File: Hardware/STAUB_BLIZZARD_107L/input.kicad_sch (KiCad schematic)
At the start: 26 parts, among them IC2 MC33978AES

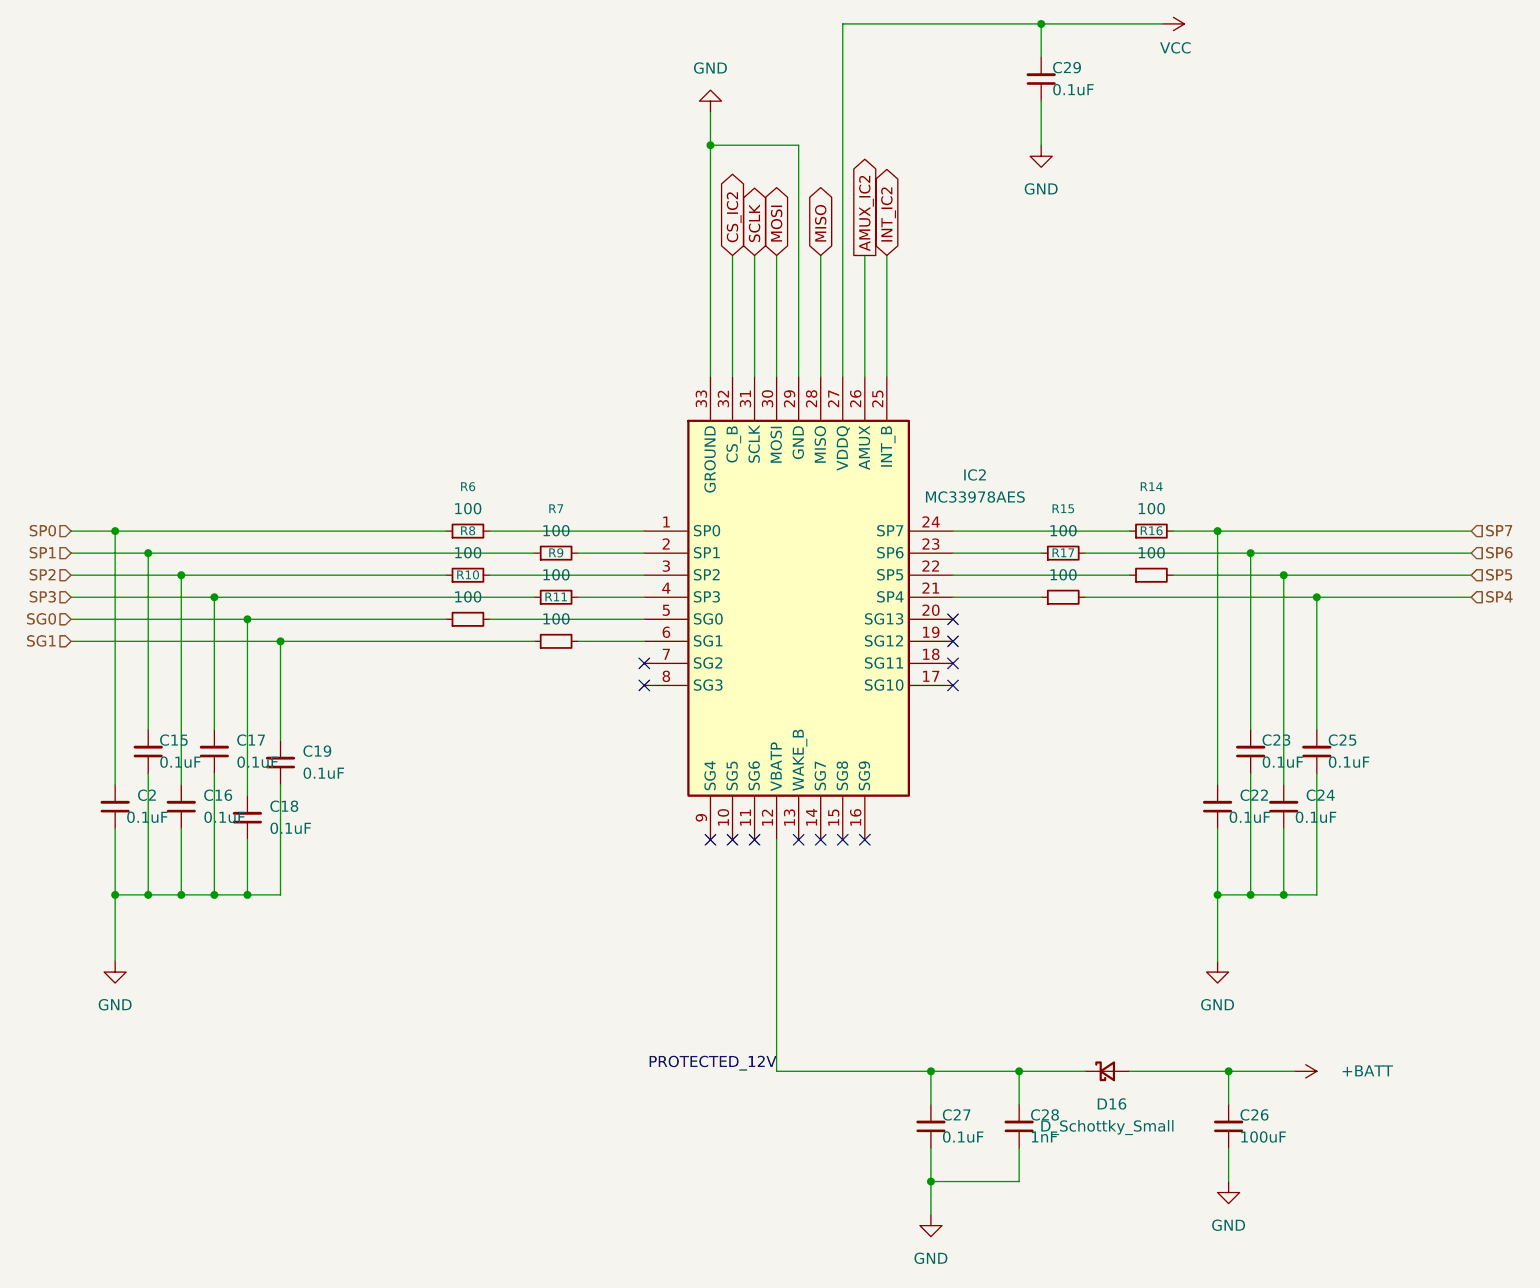
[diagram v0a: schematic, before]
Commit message: Travail sur le BOM, changement de quelques empreintes pour aligner sur les disponibilités
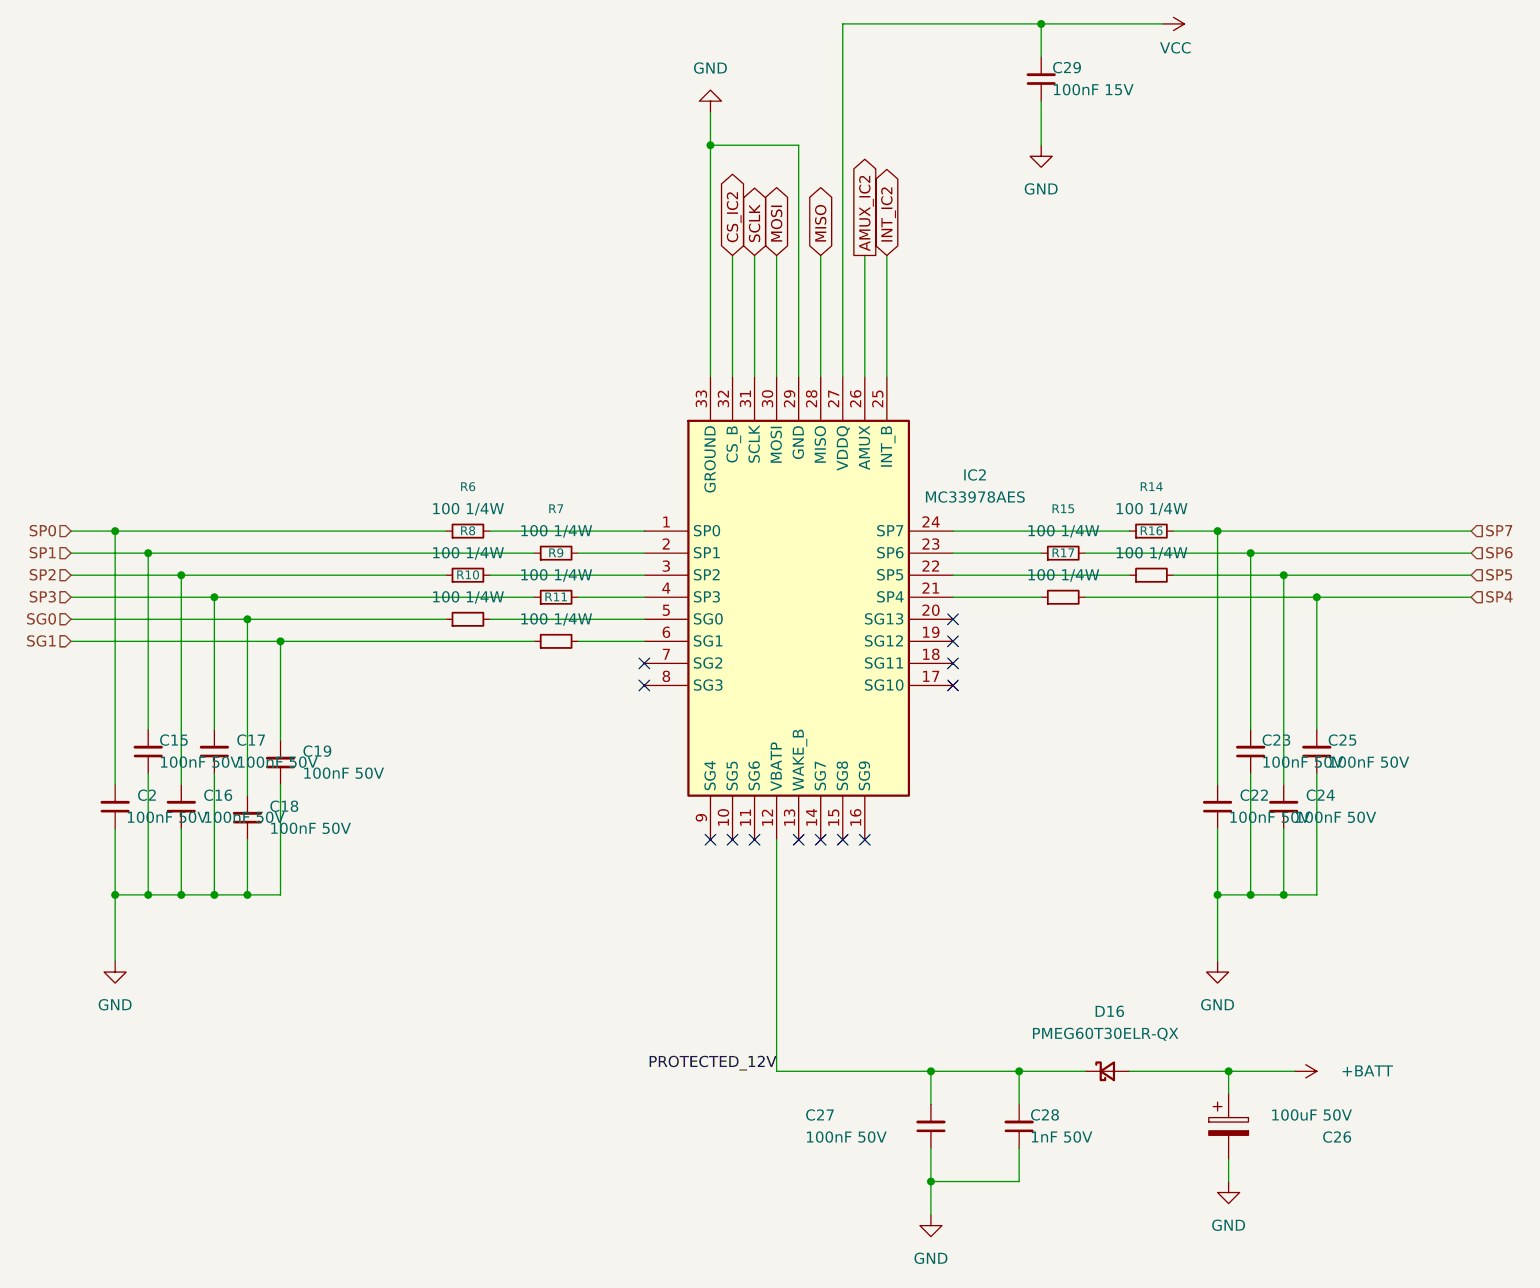
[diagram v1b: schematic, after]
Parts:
- C15, C16, C17, C18, C19, C2, C22, C23, C24, C25, C27: value 0.1uF -> 100nF 50V; footprint Capacitor_SMD:C_0402_1005Metric -> Capacitor_SMD:C_0603_1608Metric
- C26: value 100uF -> 100uF 50V; footprint Capacitor_SMD:CP_Elec_6.3x5.7 -> Capacitor_SMD:CP_Elec_8x10; symbol Device:C_Small -> Device:C_Polarized
- C28: value 1nF -> 1nF 50V
- C29: value 0.1uF -> 100nF 15V
- D16: value D_Schottky_Small -> PMEG60T30ELR-QX
- IC2: footprint SamacSys_Parts:QFN50P500X500X90-33N-D -> Custom:QFN50P500X500X90-33N-D_Pasta
- R10, R11, R14, R15, R16, R17, R6, R7, R8, R9: value 100 -> 100 1/4W
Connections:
- net +BATT: now also C26.1; no longer C26.2
- net GND: now also C26.2; no longer C26.1
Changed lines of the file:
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@@
 	)
 	(junction
-		(at 200.66 147.32)
-		(diameter 0)
-		(color 0 0 0 0)
-	)
-	(junction
 		(at 140.97 40.64)
 		(diameter 0)
@@
 	)
 	(junction
+		(at 200.66 147.32)
+		(diameter 0)
+		(color 0 0 0 0)
+	)
+	(junction
 		(at 199.39 85.09)
 		(diameter 0)
@@
 	(wire
 		(pts
+			(xy 200.66 147.32) (xy 208.28 147.32)
+		)
+		(stroke
+			(width 0)
+			(type default)
+		)
+	)
+	(wire
+		(pts
 			(xy 210.82 113.03) (xy 210.82 127)
 		)
@@
 	(wire
 		(pts
+			(xy 200.66 157.48) (xy 200.66 160.02)
+		)
+		(stroke
+			(width 0)
+			(type default)
+		)
+	)
+	(wire
+		(pts
 			(xy 153.67 53.34) (xy 153.67 67.31)
 		)
@@
 	(wire
 		(pts
-			(xy 200.66 160.02) (xy 200.66 156.21)
-		)
-		(stroke
-			(width 0)
-			(type default)
-		)
-	)
-	(wire
-		(pts
 			(xy 87.63 95.25) (xy 110.49 95.25)
 		)
@@
 	(wire
 		(pts
-			(xy 200.66 147.32) (xy 208.28 147.32)
+			(xy 166.37 160.02) (xy 176.53 160.02)
 		)
 		(stroke
@@
 	(wire
 		(pts
-			(xy 166.37 160.02) (xy 176.53 160.02)
+			(xy 151.13 67.31) (xy 151.13 40.64)
 		)
 		(stroke
@@
 	(wire
 		(pts
-			(xy 151.13 67.31) (xy 151.13 40.64)
+			(xy 67.31 97.79) (xy 91.44 97.79)
 		)
 		(stroke
@@
 	(wire
 		(pts
-			(xy 67.31 97.79) (xy 91.44 97.79)
+			(xy 200.66 147.32) (xy 200.66 149.86)
 		)
 		(stroke
@@
 	(wire
 		(pts
-			(xy 200.66 151.13) (xy 200.66 147.32)
-		)
-		(stroke
-			(width 0)
-			(type default)
-		)
-	)
-	(wire
-		(pts
 			(xy 80.01 90.17) (xy 80.01 114.3)
 		)
@@
 			)
 		)
-		(property "Value" "100"
+		(property "Value" "100 1/4W"
 			(at 123.19 85.09 90)
 			(show_name no)
@@
 			)
 		)
-		(property "Value" "100"
+		(property "Value" "100 1/4W"
 			(at 113.03 92.71 90)
 			(show_name no)
@@
 			)
 		)
-		(property "Value" "100"
+		(property "Value" "100 1/4W"
 			(at 123.19 95.25 90)
 			(show_name no)
@@
 			)
 		)
-		(property "Value" "0.1uF"
+		(property "Value" "100nF 50V"
 			(at 82.55 118.1035 0)
 			(show_name no)
@@
 			)
 		)
-		(property "Footprint" "Capacitor_SMD:C_0402_1005Metric"
+		(property "Footprint" "Capacitor_SMD:C_0603_1608Metric"
 			(at 80.01 116.84 0)
 			(hide yes)
@@
 			)
 		)
-		(property "Value" "0.1uF"
+		(property "Value" "100nF 50V"
 			(at 212.09 111.7535 0)
 			(show_name no)
@@
 			)
 		)
-		(property "Footprint" "Capacitor_SMD:C_0402_1005Metric"
+		(property "Footprint" "Capacitor_SMD:C_0603_1608Metric"
 			(at 210.82 110.49 0)
 			(hide yes)
@@
 			)
 		)
-		(property "Value" "0.1uF"
+		(property "Value" "100nF 50V"
 			(at 77.47 111.7535 0)
 			(show_name no)
@@
 			)
 		)
-		(property "Footprint" "Capacitor_SMD:C_0402_1005Metric"
+		(property "Footprint" "Capacitor_SMD:C_0603_1608Metric"
 			(at 76.2 110.49 0)
 			(hide yes)
@@
 			)
 		)
-		(property "Value" "0.1uF"
+		(property "Value" "100nF 50V"
 			(at 93.98 113.0235 0)
 			(show_name no)
@@
 			)
 		)
-		(property "Footprint" "Capacitor_SMD:C_0402_1005Metric"
+		(property "Footprint" "Capacitor_SMD:C_0603_1608Metric"
 			(at 91.44 111.76 0)
 			(hide yes)
@@
 			)
 		)
-		(property "Value" "100"
+		(property "Value" "100 1/4W"
 			(at 191.77 87.63 90)
 			(show_name no)
@@
 			)
 		)
-		(property "Value" "0.1uF"
+		(property "Value" "100nF 50V"
 			(at 204.47 111.7535 0)
 			(show_name no)
@@
 			)
 		)
-		(property "Footprint" "Capacitor_SMD:C_0402_1005Metric"
+		(property "Footprint" "Capacitor_SMD:C_0603_1608Metric"
 			(at 203.2 110.49 0)
 			(hide yes)
@@
 		(dnp no)
 		(property "Reference" "C27"
-			(at 167.64 152.3935 0)
+			(at 151.892 152.4 0)
 			(show_name no)
 			(do_not_autoplace no)
@@
 			)
 		)
-		(property "Value" "0.1uF"
-			(at 167.64 154.9335 0)
+		(property "Value" "100nF 50V"
+			(at 151.892 154.94 0)
 			(show_name no)
 			(do_not_autoplace no)
@@
 			)
 		)
-		(property "Footprint" "Capacitor_SMD:C_0402_1005Metric"
+		(property "Footprint" "Capacitor_SMD:C_0603_1608Metric"
 			(at 166.37 153.67 0)
 			(hide yes)
@@
 			)
 		)
-		(property "Value" "100"
+		(property "Value" "100 1/4W"
 			(at 181.61 90.17 90)
 			(show_name no)
@@
 			)
 		)
-		(property "Value" "1nF"
+		(property "Value" "1nF 50V"
 			(at 177.8 154.9335 0)
 			(show_name no)
@@
 			)
 		)
-		(property "Value" "0.1uF"
+		(property "Value" "100nF 15V"
 			(at 180.34 34.2835 0)
 			(show_name no)
@@
 			)
 		)
-		(property "Value" "0.1uF"
+		(property "Value" "100nF 50V"
 			(at 208.28 118.1035 0)
 			(show_name no)
@@
 			)
 		)
-		(property "Footprint" "Capacitor_SMD:C_0402_1005Metric"
+		(property "Footprint" "Capacitor_SMD:C_0603_1608Metric"
 			(at 207.01 116.84 0)
 			(hide yes)
@@
 			)
 		)
-		(property "Value" "0.1uF"
+		(property "Value" "100nF 50V"
 			(at 86.36 111.7535 0)
 			(show_name no)
@@
 			)
 		)
-		(property "Footprint" "Capacitor_SMD:C_0402_1005Metric"
+		(property "Footprint" "Capacitor_SMD:C_0603_1608Metric"
 			(at 83.82 110.49 0)
 			(hide yes)
@@
 			)
 		)
-		(property "Value" "100"
+		(property "Value" "100 1/4W"
 			(at 113.03 82.55 90)
 			(show_name no)
@@
 	)
 	(symbol
-		(lib_id "Device:C_Small")
-		(at 200.66 153.67 180)
+		(lib_id "Device:C_Polarized")
+		(at 200.66 153.67 0)
 		(unit 1)
 		(body_style 1)
@@
 		(dnp no)
 		(property "Reference" "C26"
-			(at 201.93 152.3935 0)
+			(at 214.884 154.94 0)
 			(show_name no)
 			(do_not_autoplace no)
@@
 			)
 		)
-		(property "Value" "100uF"
-			(at 201.93 154.9335 0)
+		(property "Value" "100uF 50V"
+			(at 214.884 152.4 0)
 			(show_name no)
 			(do_not_autoplace no)
@@
 			)
 		)
-		(property "Footprint" "Capacitor_SMD:CP_Elec_6.3x5.7"
-			(at 200.66 153.67 0)
+		(property "Footprint" "Capacitor_SMD:CP_Elec_8x10"
+			(at 201.6252 157.48 0)
 			(hide yes)
 			(show_name no)
@@
 			)
 		)
-		(property "Description" "Unpolarized capacitor, small symbol"
+		(property "Description" "GXC1V101MCW1GS"
 			(at 200.66 153.67 0)
 			(hide yes)
@@
 			)
 		)
-		(property "Value" "100"
+		(property "Value" "100 1/4W"
 			(at 113.03 87.63 90)
 			(show_name no)
@@
 			)
 		)
-		(property "Value" "0.1uF"
+		(property "Value" "100nF 50V"
 			(at 90.17 119.3735 0)
 			(show_name no)
@@
 			)
 		)
-		(property "Footprint" "Capacitor_SMD:C_0402_1005Metric"
+		(property "Footprint" "Capacitor_SMD:C_0603_1608Metric"
 			(at 87.63 118.11 0)
 			(hide yes)
@@
 			)
 		)
-		(property "Value" "100"
+		(property "Value" "100 1/4W"
 			(at 123.19 90.17 90)
 			(show_name no)
@@
 			)
 		)
-		(property "Value" "100"
+		(property "Value" "100 1/4W"
 			(at 181.61 85.09 90)
 			(show_name no)
@@
 			)
 		)
-		(property "Value" "0.1uF"
+		(property "Value" "100nF 50V"
 			(at 200.66 118.1035 0)
 			(show_name no)
@@
 			)
 		)
-		(property "Footprint" "Capacitor_SMD:C_0402_1005Metric"
+		(property "Footprint" "Capacitor_SMD:C_0603_1608Metric"
 			(at 199.39 116.84 0)
 			(hide yes)
@@
 			)
 		)
-		(property "Value" "100"
+		(property "Value" "100 1/4W"
 			(at 191.77 82.55 90)
 			(show_name no)
@@
 			)
 		)
-		(property "Value" "0.1uF"
+		(property "Value" "100nF 50V"
 			(at 73.66 118.1035 0)
 			(show_name no)
@@
 			)
 		)
-		(property "Footprint" "Capacitor_SMD:C_0402_1005Metric"
+		(property "Footprint" "Capacitor_SMD:C_0603_1608Metric"
 			(at 72.39 116.84 0)
 			(hide yes)
@@
 			)
 		)
-		(property "Footprint" "SamacSys_Parts:QFN50P500X500X90-33N-D"
+		(property "Footprint" "Custom:QFN50P500X500X90-33N-D_Pasta"
 			(at 165.1 169.85 0)
 			(hide yes)
@@
 		(dnp no)
 		(property "Reference" "D16"
-			(at 187.198 151.13 0)
+			(at 186.944 140.462 0)
 			(show_name no)
 			(do_not_autoplace no)
@@
 			)
 		)
-		(property "Value" "D_Schottky_Small"
-			(at 186.69 153.67 0)
+		(property "Value" "PMEG60T30ELR-QX"
+			(at 186.436 143.002 0)
 			(show_name no)
 			(do_not_autoplace no)

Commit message: Ajout du connecteur de programmation du module Lora
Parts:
- renumbered C2 to C20, C15 to C21, C16 to C22, C17 to C23, C18 to C24, C19 to C25, C27 to C26, C28 to C27, C29 to C28, C22 to C29, C26 to C30, C23 to C31, C24 to C32, C25 to C33, D16 to D21, IC2 to IC4, R6 to R18, R8 to R19, R10 to R20, R7 to R21, R9 to R22, R11 to R23, R15 to R24, R17 to R25, R14 to R26, R16 to R27
